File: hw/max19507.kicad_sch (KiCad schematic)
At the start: 27 parts, among them U9 MAX19517

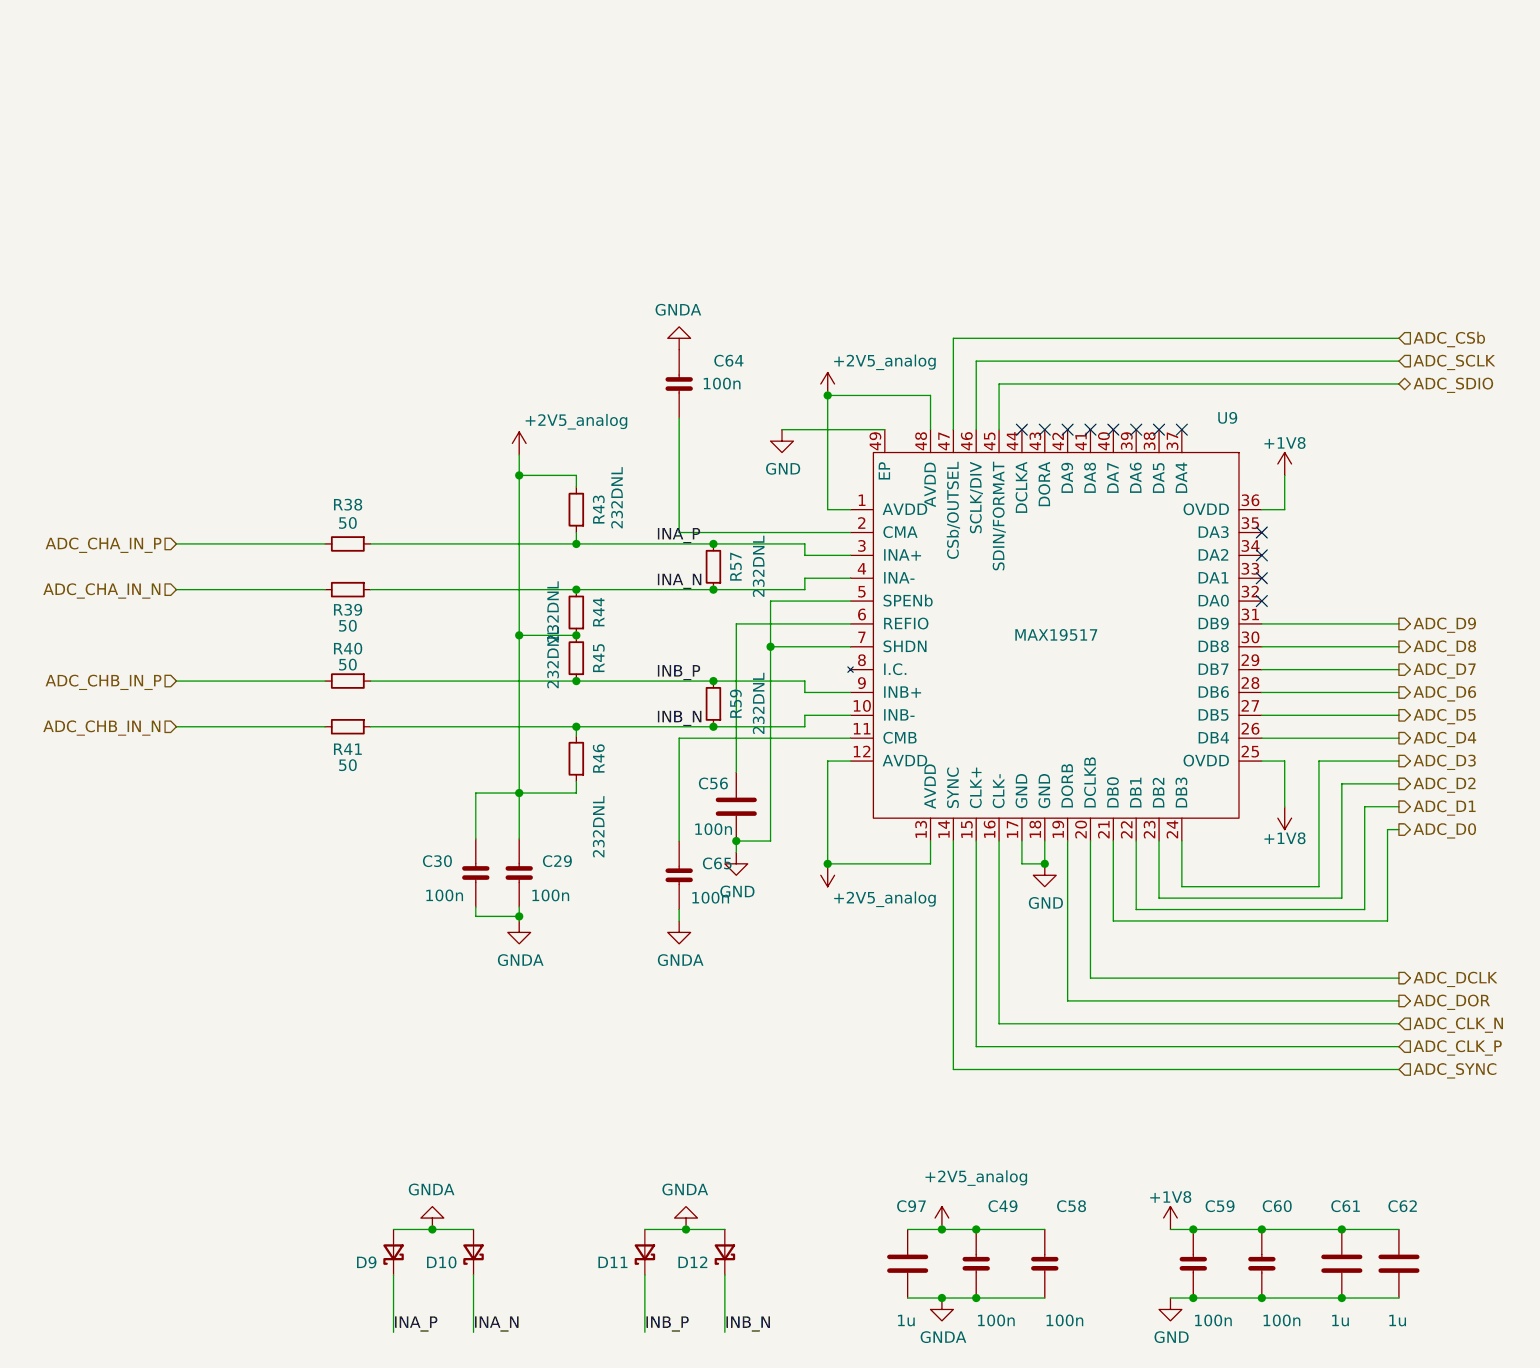
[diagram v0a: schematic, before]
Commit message: moved trion into place; going to 'hide' footprint reference designators...
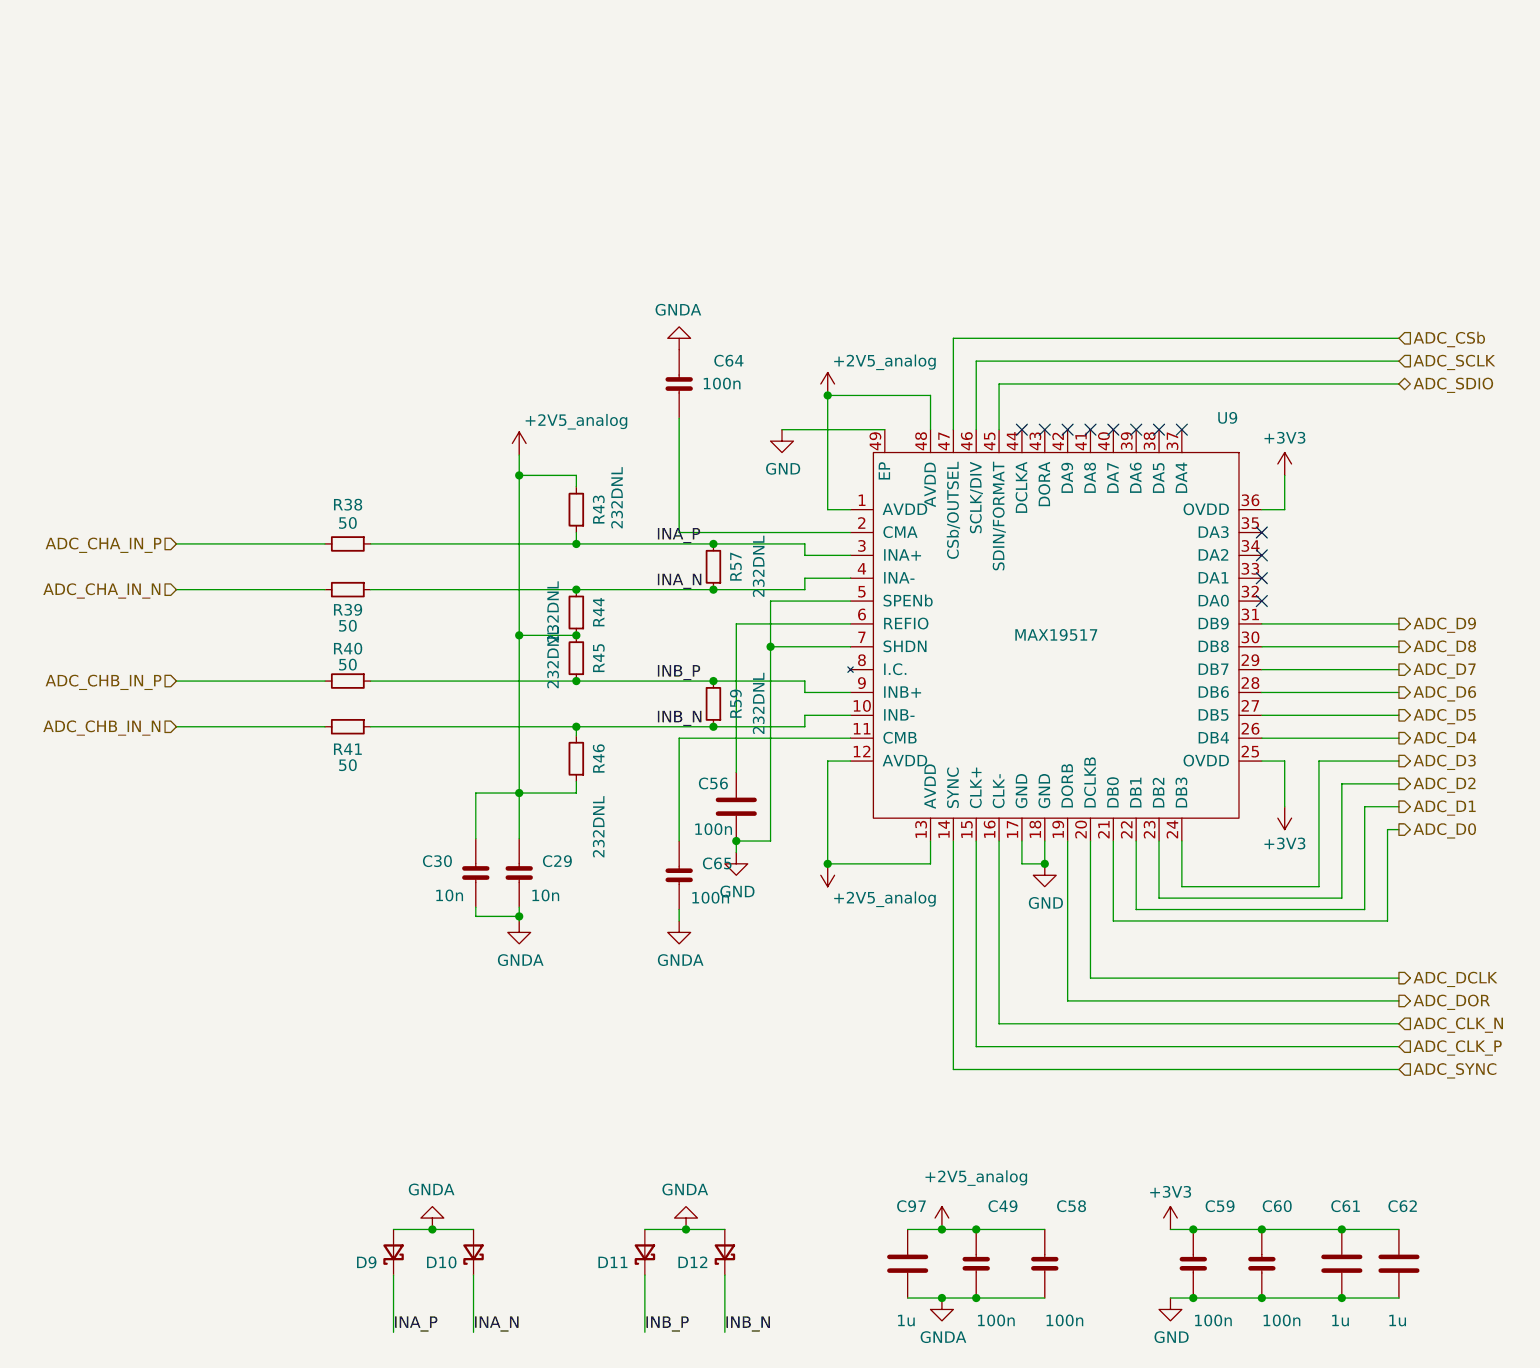
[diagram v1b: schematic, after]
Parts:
- C29, C30: value 100n -> 10n
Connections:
- net +1V8 renamed +3V3

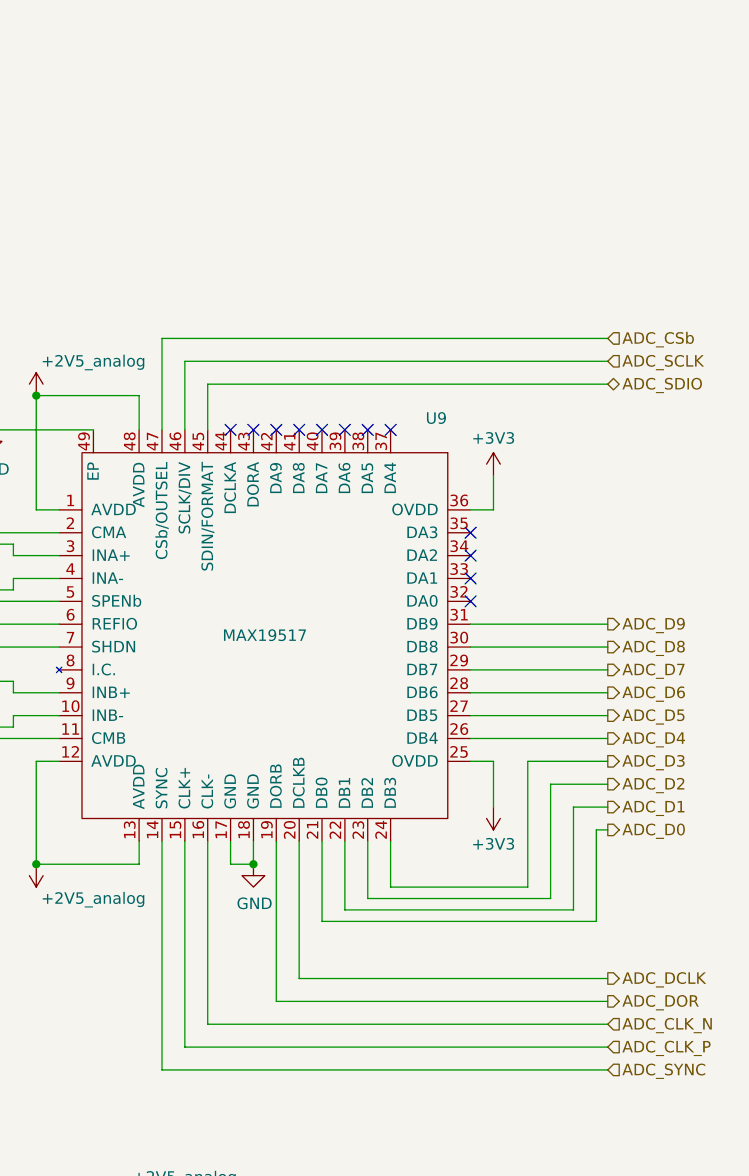
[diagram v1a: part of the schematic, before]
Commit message: layout almost complete with UPLI on the RHS => NO CLOCK INPUT
Have to rework and move the usb transceiver to the left...
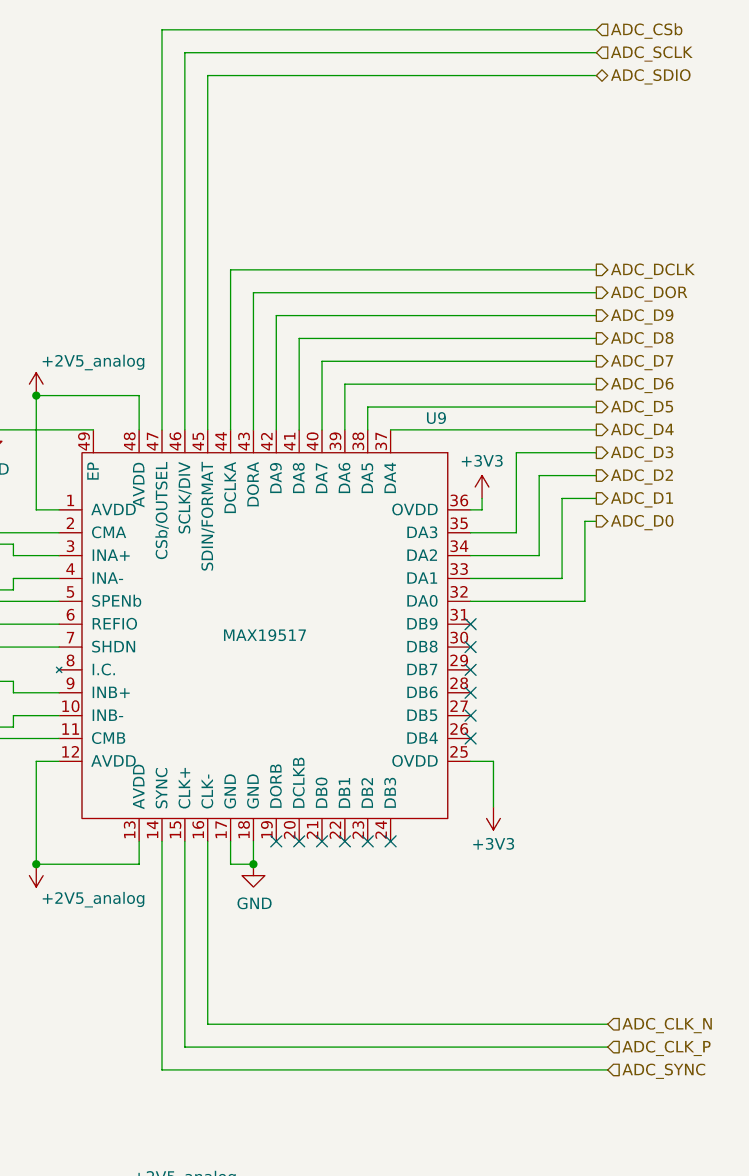
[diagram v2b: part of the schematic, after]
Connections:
- net ADC_D0: now also U9.32 (DA0); no longer U9.21 (DB0)
- net ADC_D1: now also U9.33 (DA1); no longer U9.22 (DB1)
- net ADC_D2: now also U9.34 (DA2); no longer U9.23 (DB2)
- net ADC_D3: now also U9.35 (DA3); no longer U9.24 (DB3)
- net ADC_D4: now also U9.37 (DA4); no longer U9.26 (DB4)
- net ADC_D5: now also U9.38 (DA5); no longer U9.27 (DB5)
- net ADC_D6: now also U9.39 (DA6); no longer U9.28 (DB6)
- net ADC_D7: now also U9.40 (DA7); no longer U9.29 (DB7)
- net ADC_D8: now also U9.41 (DA8); no longer U9.30 (DB8)
- net ADC_D9: now also U9.42 (DA9); no longer U9.31 (DB9)
- net ADC_DCLK: now also U9.44 (DCLKA); no longer U9.20 (DCLKB)
- net ADC_DOR: now also U9.43 (DORA); no longer U9.19 (DORB)

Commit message: finalizing...
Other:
- moved on the sheet: C29, C30, R46

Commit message: WIP; converging
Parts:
- added C34, C35: 10n, Capacitor_SMD:C_0603_1608Metric, symbol fmc:100nF_402
- added R36, R37, R77, R78: 301, Resistor_SMD:R_0603_1608Metric, symbol Device:R_Small
- R38, R39, R40, R41: value 50 -> 75
- R43, R44, R45, R46: value 232DNL -> 226
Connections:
- net ADC_CHA_IN_N: now also R37.2
- net ADC_CHA_IN_P: now also R36.1
- net ADC_CHB_IN_N: now also R78.2
- net ADC_CHB_IN_P: now also R77.1
- net GNDA: now also C34.2, C35.2
- new net -2V5_analog: C34.1, C35.1, R36.2, R37.1, R77.2, R78.1

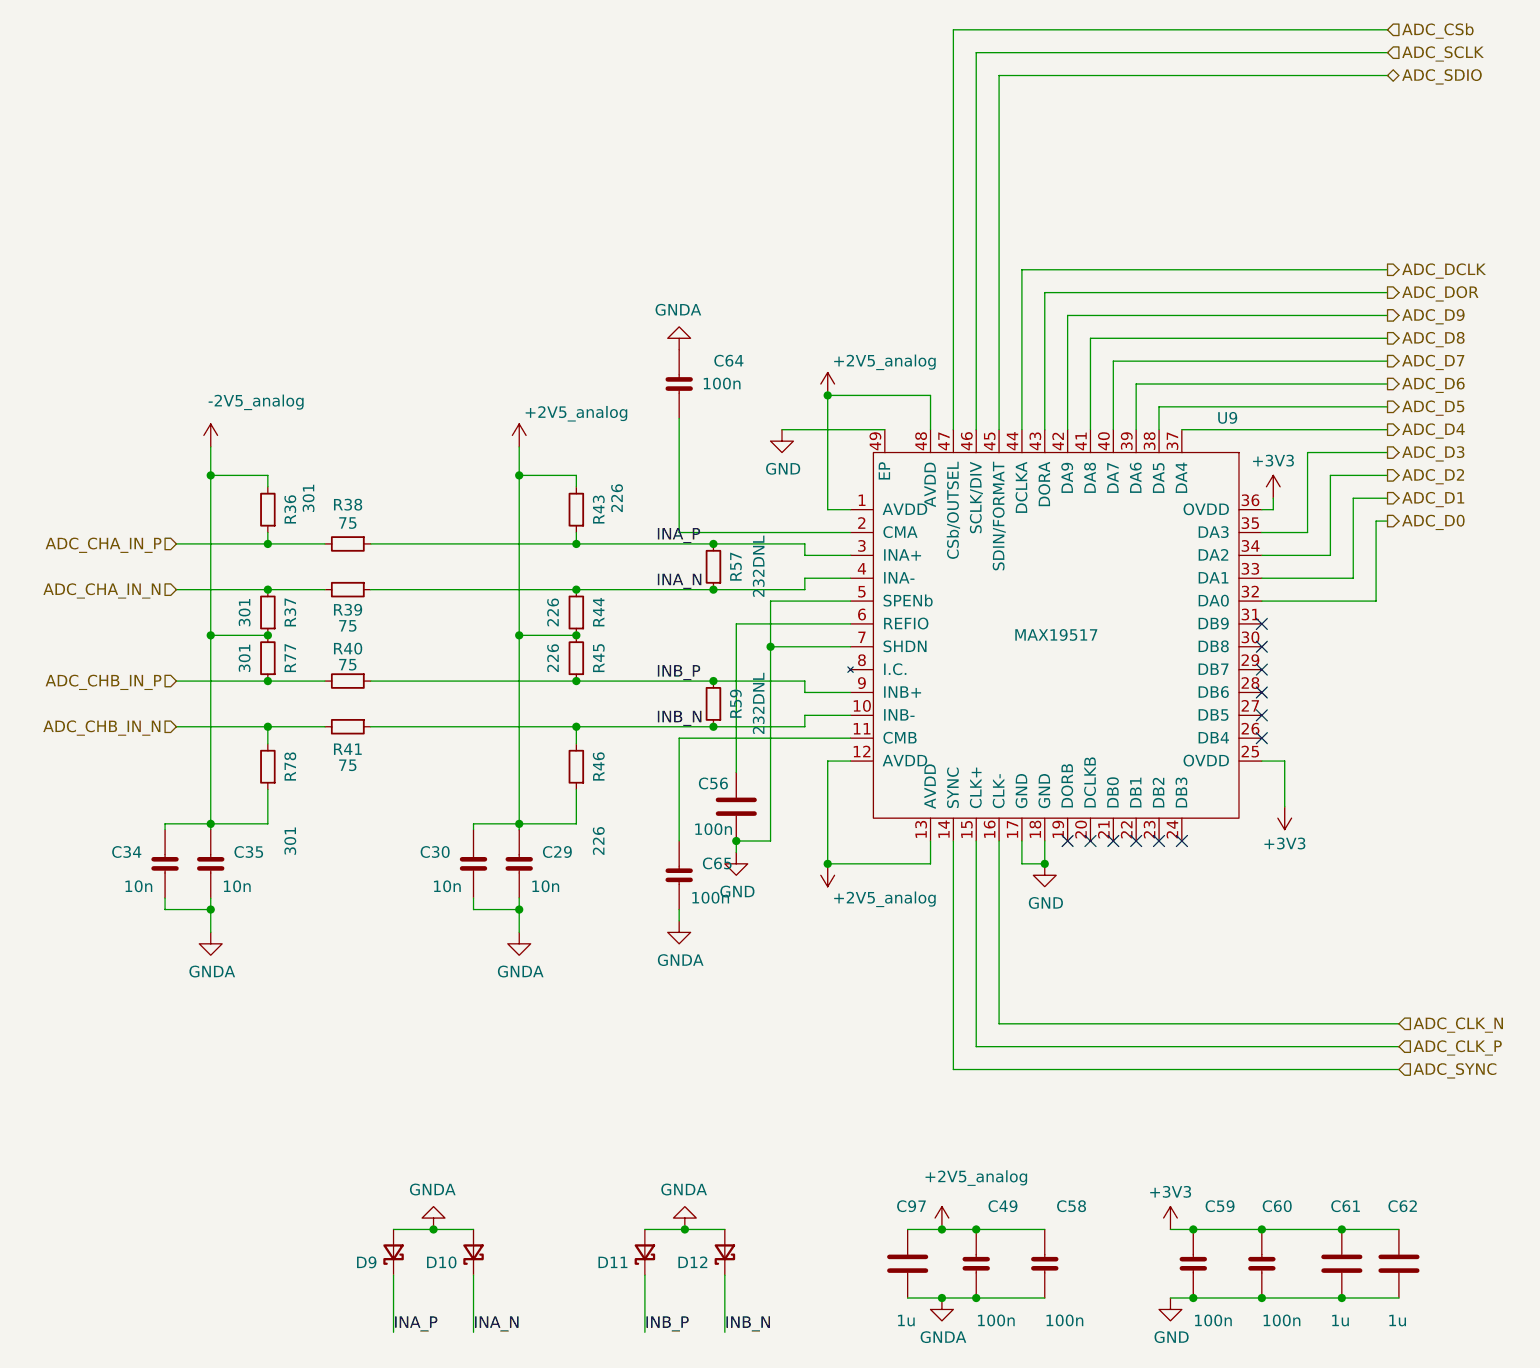
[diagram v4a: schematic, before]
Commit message: consolidated components to simplify BOM
(nothing actually changed but the symbols representing identical
components are now identical -> no more multiple BOM entries for
the same type of component).
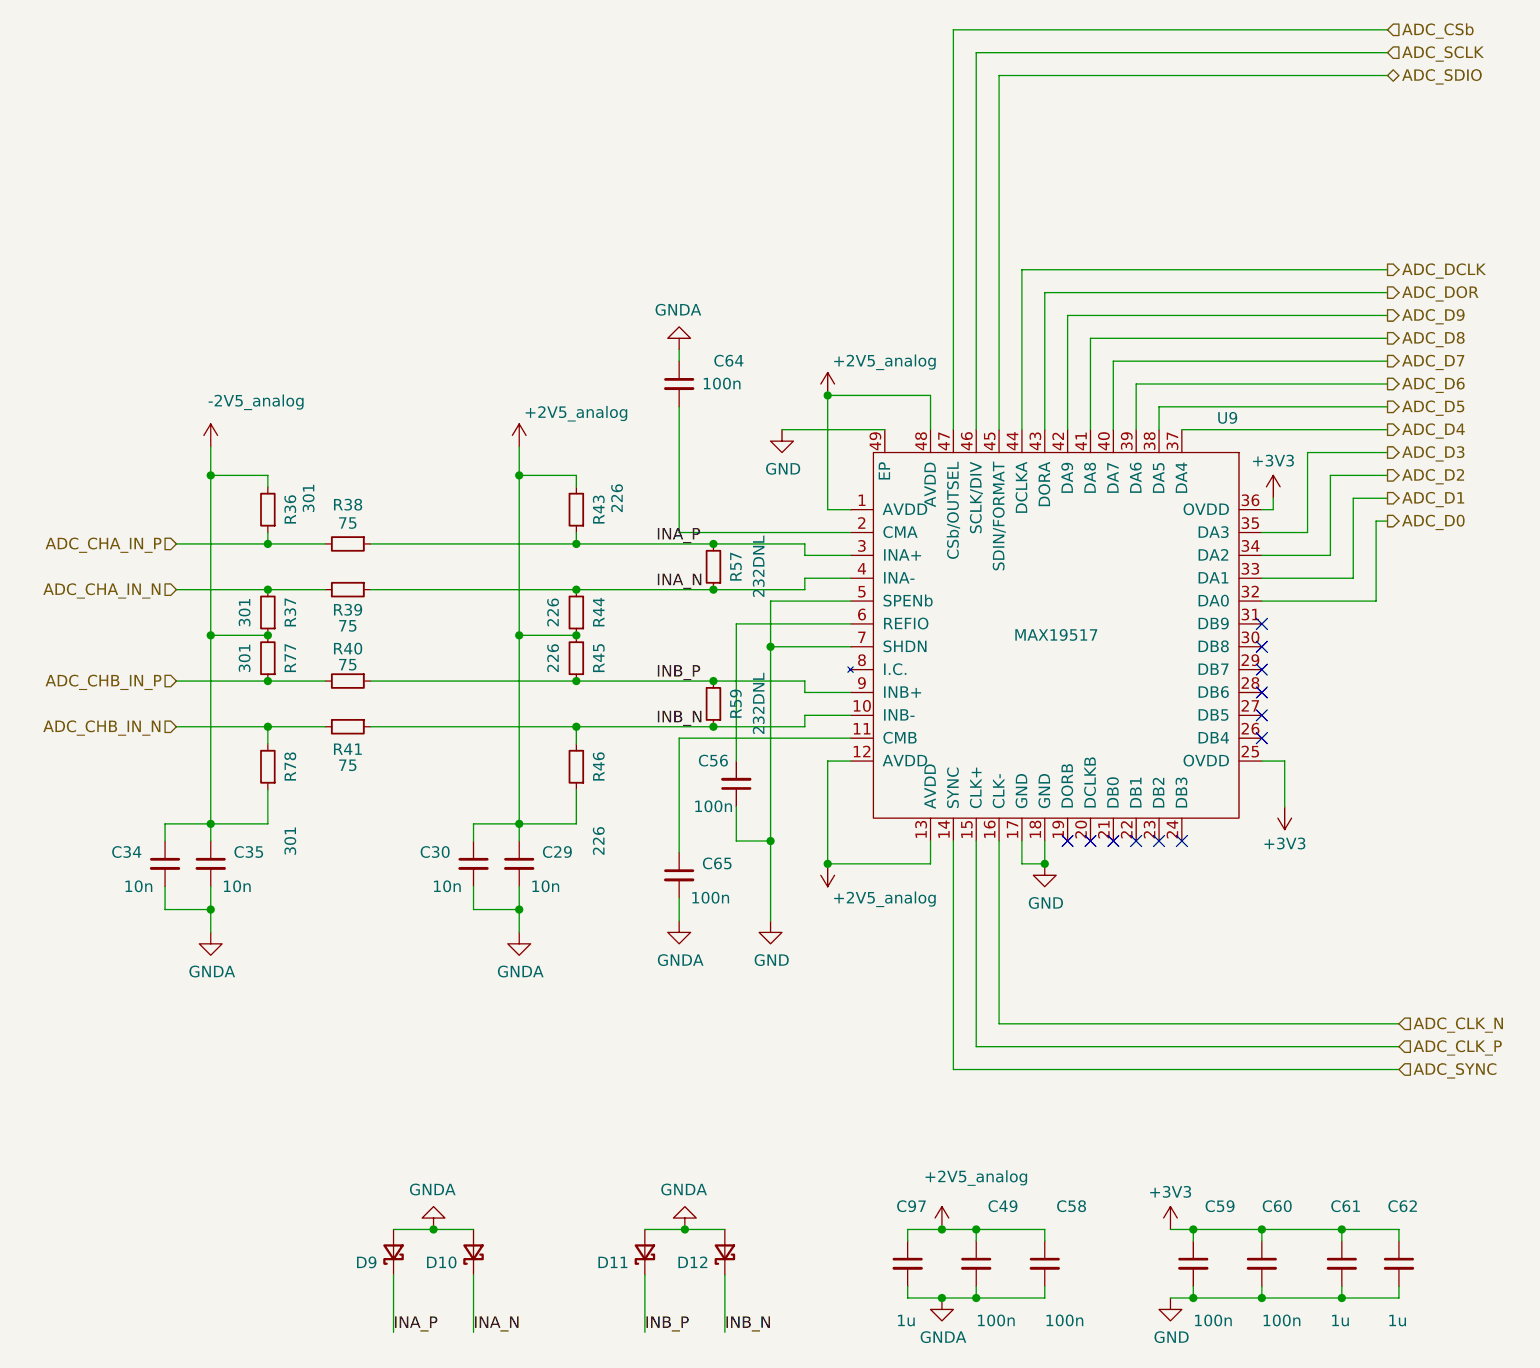
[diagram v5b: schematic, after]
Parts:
- C29, C30, C34, C35, C49, C58, C59, C60: symbol fmc:100nF_402 -> Device:C_Small
- C56: symbol fmc:100nF_603 -> Device:C_Small; Manufacturer (none) -> Samsung; Part (none) -> CL10B104KB8NFN
- C61, C62, C97: symbol fmc:1uF_805 -> Device:C_Small; Manufacturer (none) -> TDK; Part (none) -> CGA4J2X7R1C105K125AA
- C64, C65: symbol fmc:100nF_402 -> Device:C_Small; Manufacturer (none) -> Samsung; Part (none) -> CL10B104KB8NFN
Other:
- moved on the sheet: C56
